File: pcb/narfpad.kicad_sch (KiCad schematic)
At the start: 26 parts, among them SW1 SW_Push, SW2 SW_Push, SW3 SW_Push, SW4 SW_Push, SW5 SW_Push, SW6 SW_Push, SW7 SW_Push, SW8 SW_Push, SW9 SW_Push, U1 xiao

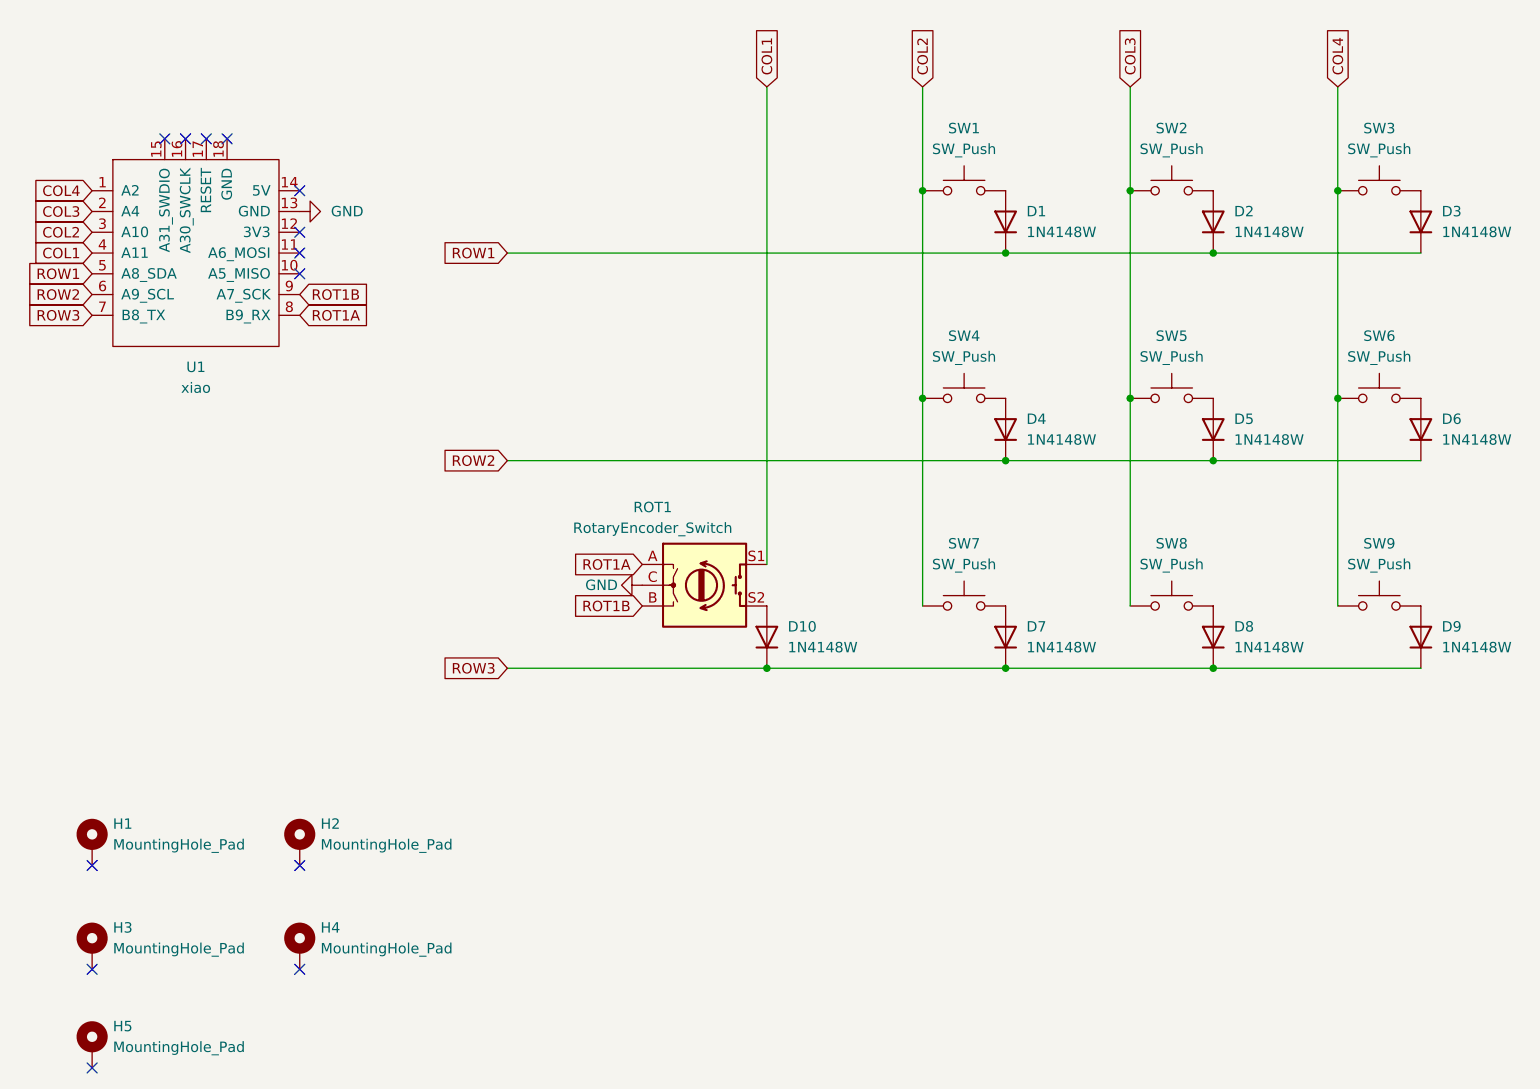
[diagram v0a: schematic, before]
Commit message: Initial Neopixel Integration
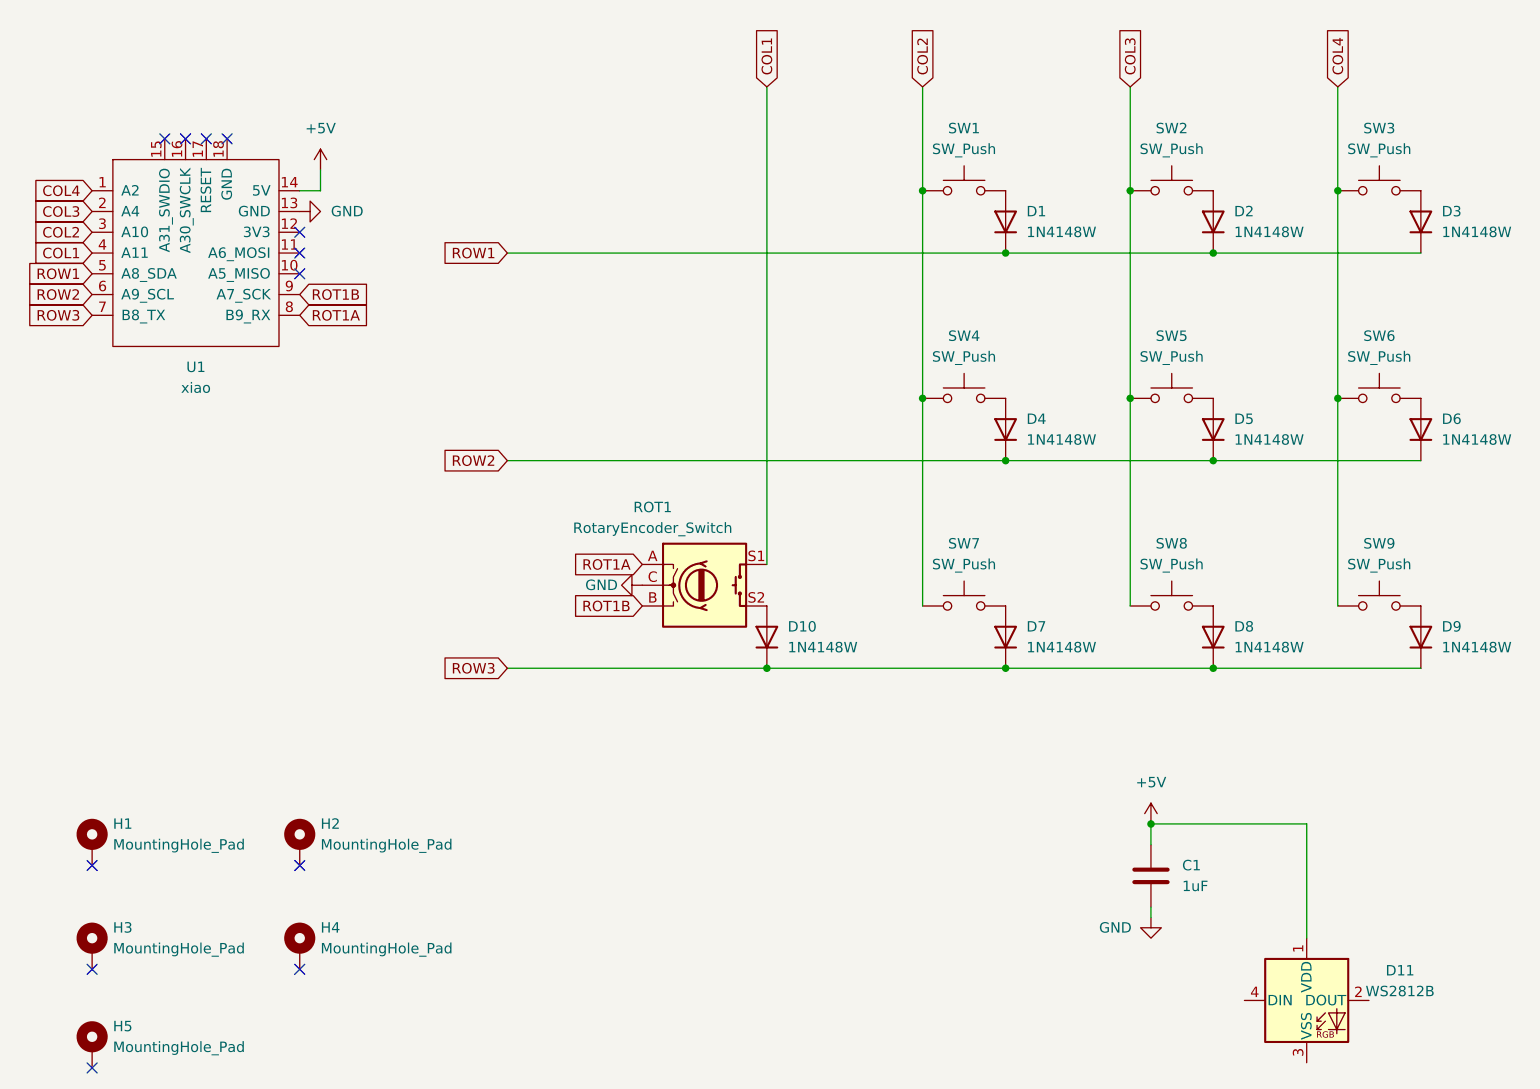
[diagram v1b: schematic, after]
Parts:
- added C1: 1uF, symbol Device:C
- added D11: WS2812B, LED_SMD:LED_WS2812B_PLCC4_5.0x5.0mm_P3.2mm, symbol LED:WS2812B
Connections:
- net GND: now also C1.2
- net +5V: now reaches U1.14 (5V)
- net +5V: now also C1.1, D11.1 (VDD)
- no-connect marks 13 -> 12
